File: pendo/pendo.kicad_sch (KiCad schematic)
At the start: 23 parts, among them J1 M2, J2 M1, J3 Motor Vin, J4 Conn_ARM_JTAG_SWD_10, SW1 SW_Push, U1 STM32G431RBTx, U2 DRV8870DDA, U3 DRV8870DDA, U4 ESP32-C3-WROOM-02, U5 AP2112K-3.3

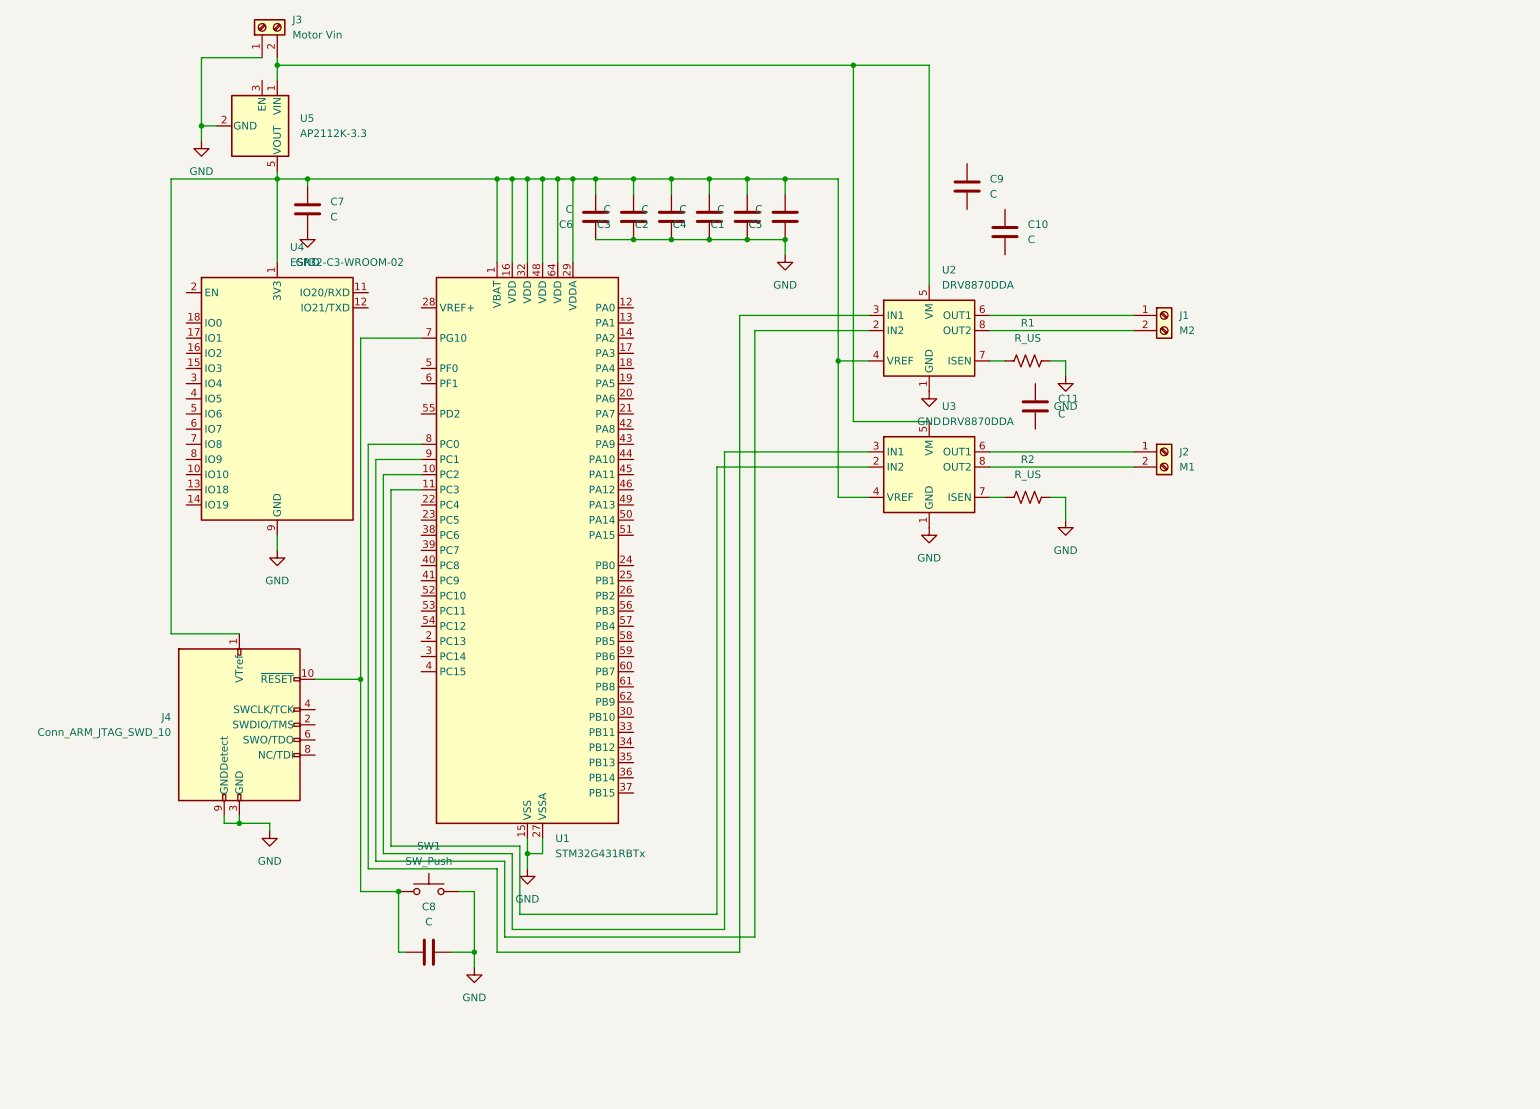
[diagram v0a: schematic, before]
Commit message: added caps and resistor values
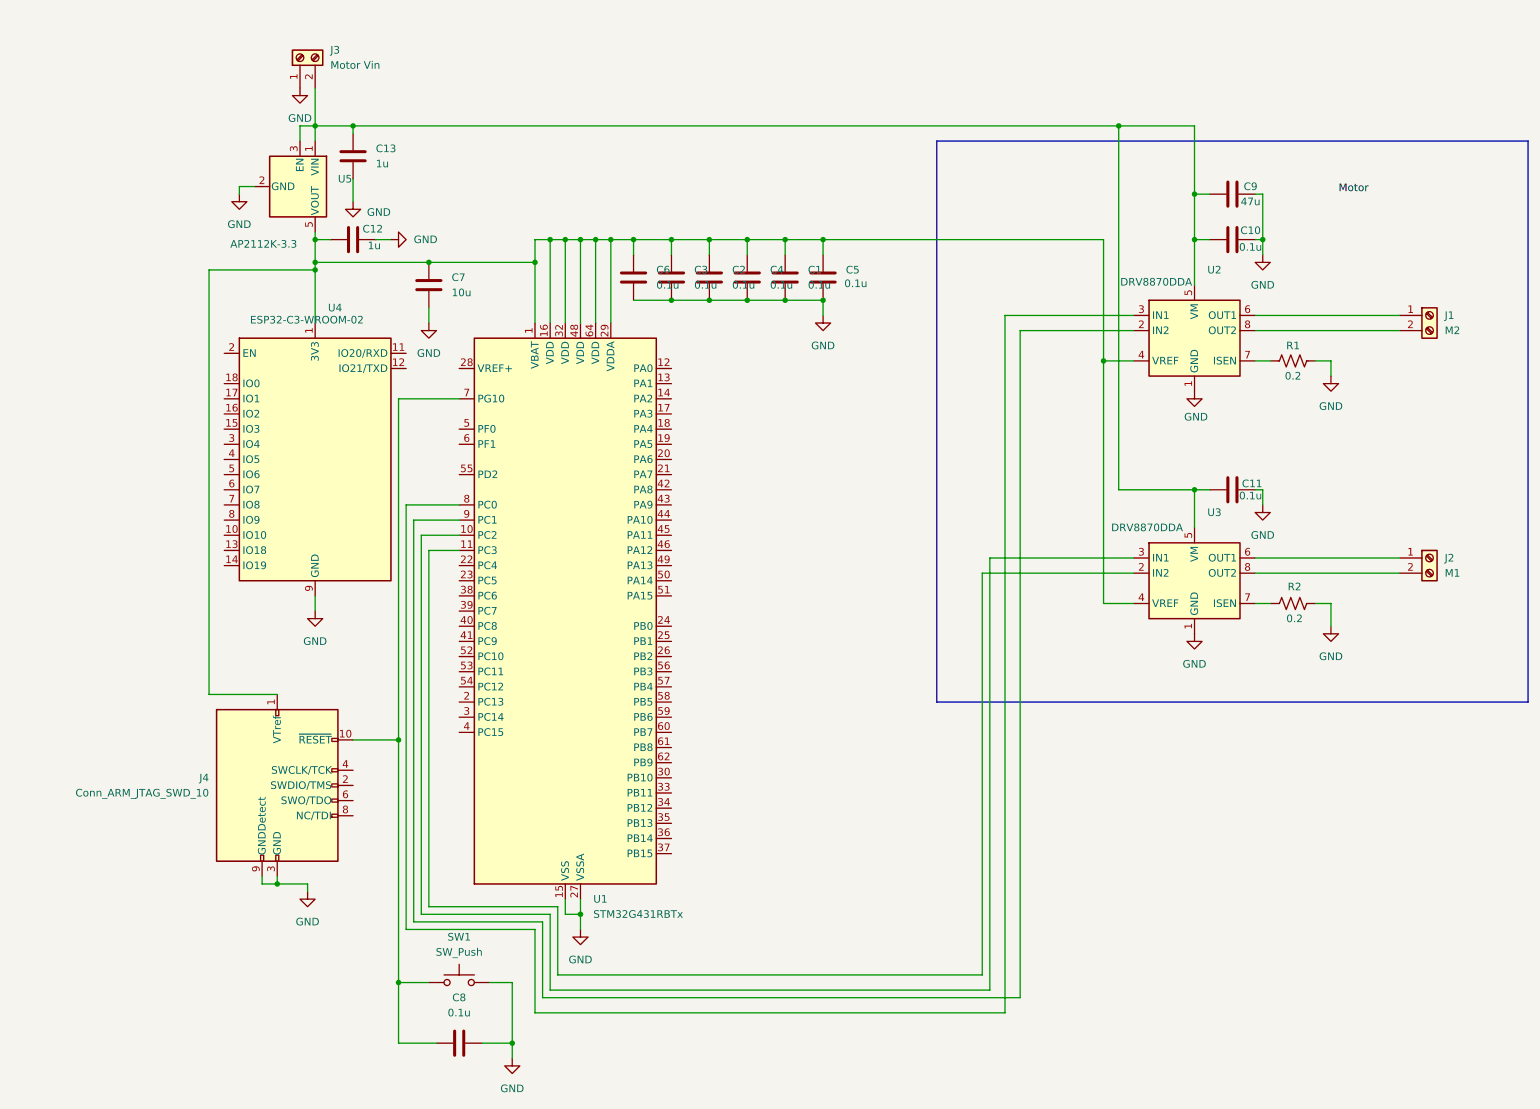
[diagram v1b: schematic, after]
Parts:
- added C12, C13: 1u, symbol Device:C
- C1, C10, C11, C2, C3, C4, C5, C6, C8: value C -> 0.1u
- C7: value C -> 10u
- C9: value C -> 47u
- R1, R2: value R_US -> 0.2
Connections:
- net GND: now also C10.2, C11.2, C9.2, C12.2, C13.2
- net at C1.2, C2.2, C3.2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: now also C12.1
- net at J3.2 (Pin_2), U2.5 (VM), U3.5 (VM)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: now also C10.1, C11.1, C9.1, U5.3 (EN), C13.1
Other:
- moved on the sheet: C1, C10, C11, C2, C3, C4, C5, C6, C7, C8, C9, J1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

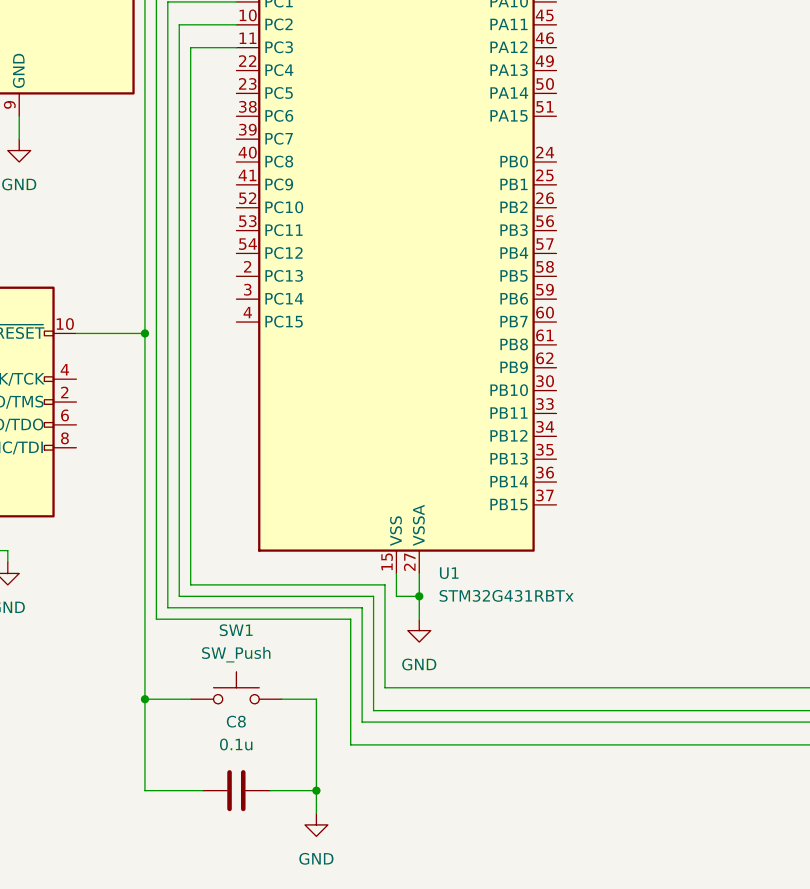
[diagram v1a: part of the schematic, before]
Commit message: adding i2c
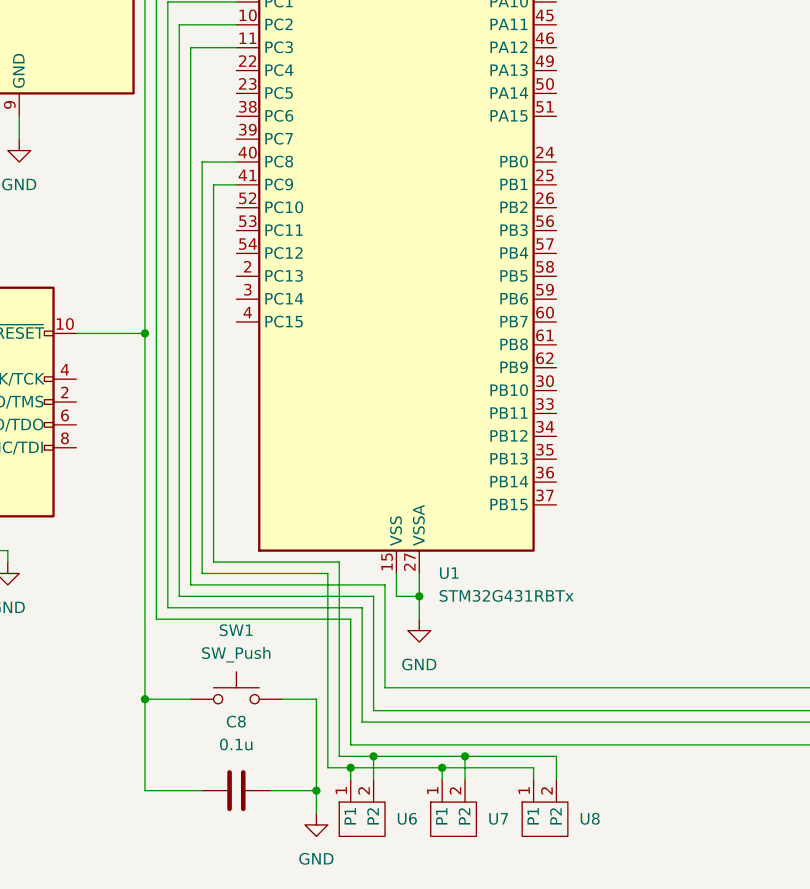
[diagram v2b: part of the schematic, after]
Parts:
- added U6, U7, U8: (no value), symbol Terminals:2pin
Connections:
- net at U1.40 (PC8): now also U6.1 (P1), U7.1 (P1), U8.1 (P1)
- net at U1.41 (PC9): now also U6.2 (P2), U7.2 (P2), U8.2 (P2)

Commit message: plane pours
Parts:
- C1, C12, C2, C3, C4, C5, C6, C7, C8: footprint (none) -> Capacitor_SMD:C_0603_1608Metric
- C10, C11, C13, C9: footprint (none) -> Capacitor_SMD:C_1206_3216Metric
- J1, J2, J3: footprint (none) -> TerminalBlock:TerminalBlock_MaiXu_MX126-5.0-02P_1x02_P5.00mm
- J4: footprint (none) -> Connector_PinHeader_1.27mm:PinHeader_2x05_P1.27mm_Vertical_SMD
- R1, R2: footprint (none) -> Resistor_SMD:R_0603_1608Metric
- SW1: footprint (none) -> Button_Switch_THT:SW_PUSH_6mm
- U6, U7, U8: footprint (none) -> Connector_PinHeader_2.54mm:PinHeader_1x02_P2.54mm_Vertical
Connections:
- net +3.3V: now reaches C1.2, C12.1, C2.2, C3.2, C4.2, C5.2, C6.2, C7.1, J4.1 (VTref), U1.1 (VBAT), U1.16 (VDD), U1.29 (VDDA), U1.32 (VDD), U1.48 (VDD), U1.64 (VDD), U2.4 (VREF), U3.4 (VREF), U4.1 (3V3), U5.5 (VOUT)
- net +12V: now reaches C10.1, C11.1, C13.1, C9.1, J3.2 (Pin_2), U2.5 (VM), U3.5 (VM), U5.1 (VIN), U5.3 (EN)

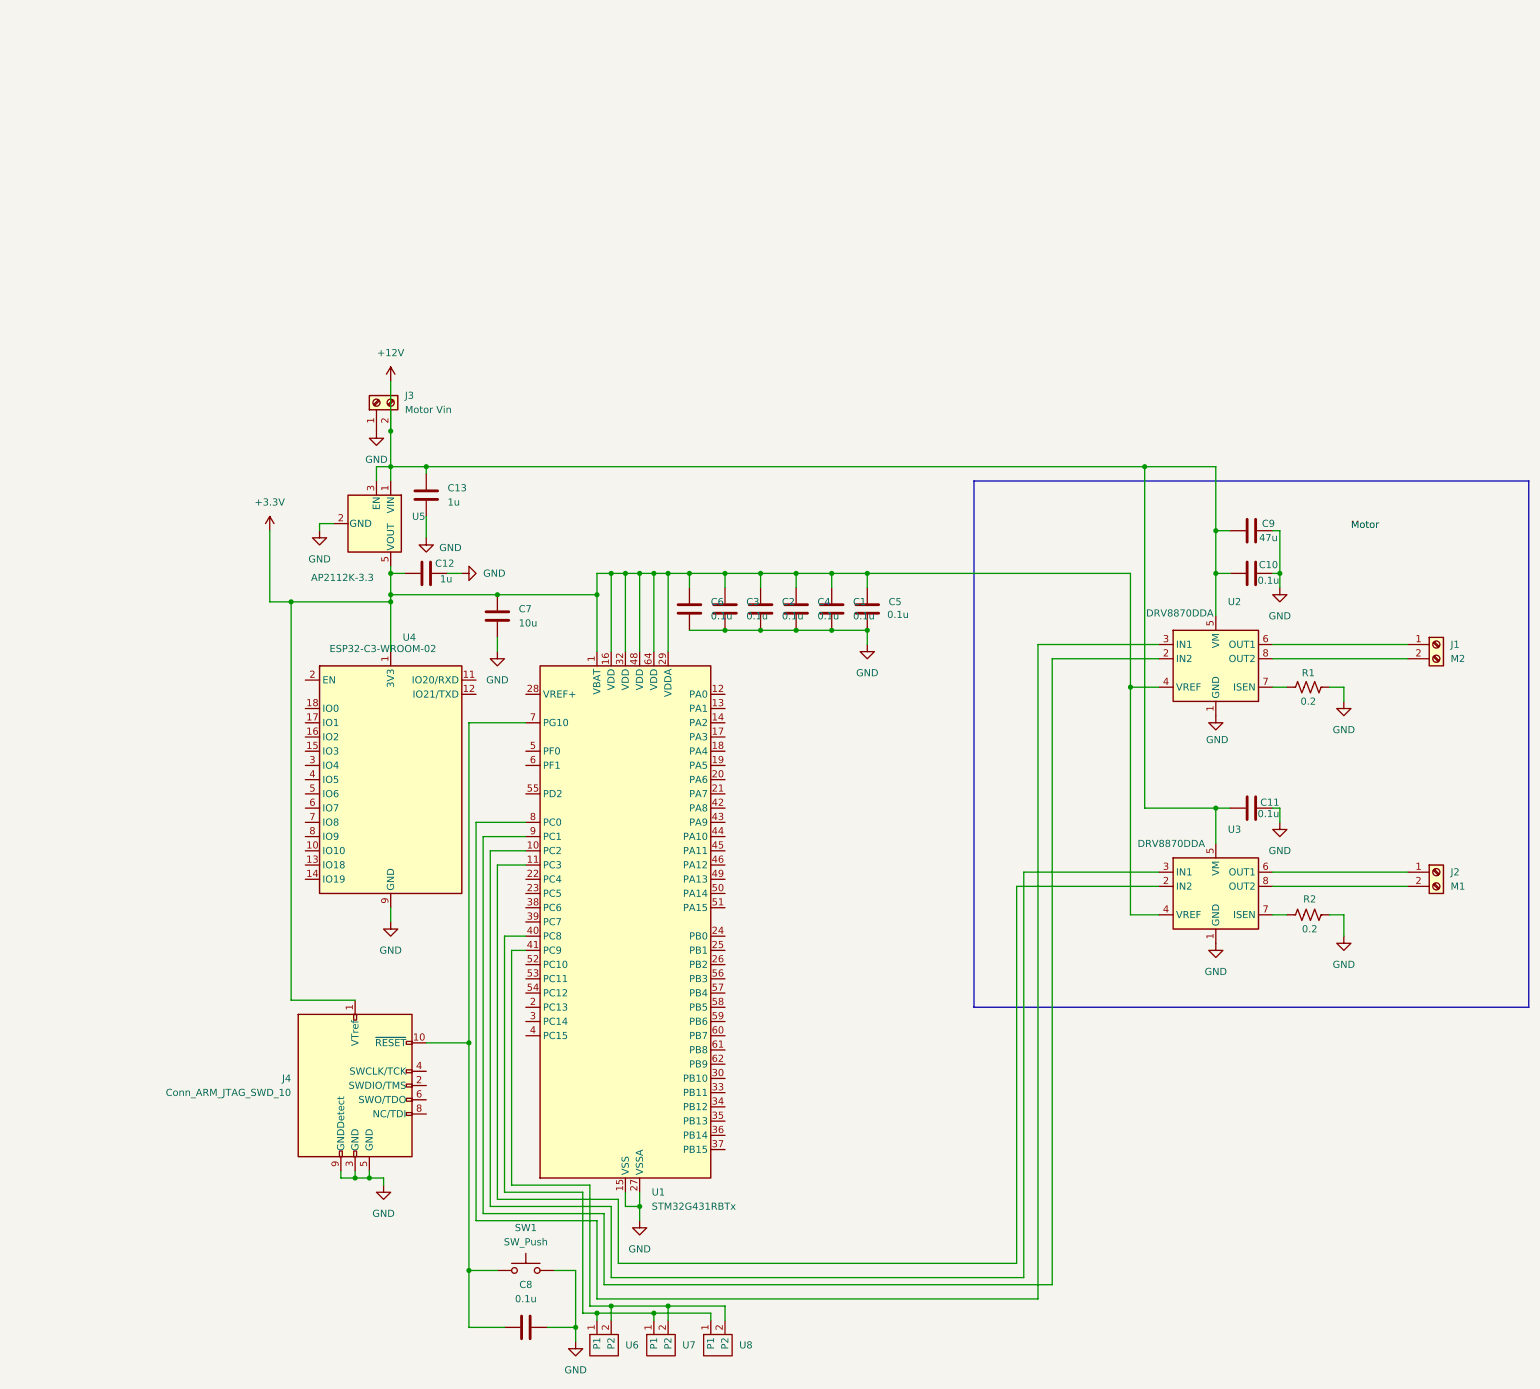
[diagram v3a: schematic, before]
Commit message: started gerber redesign + update power components
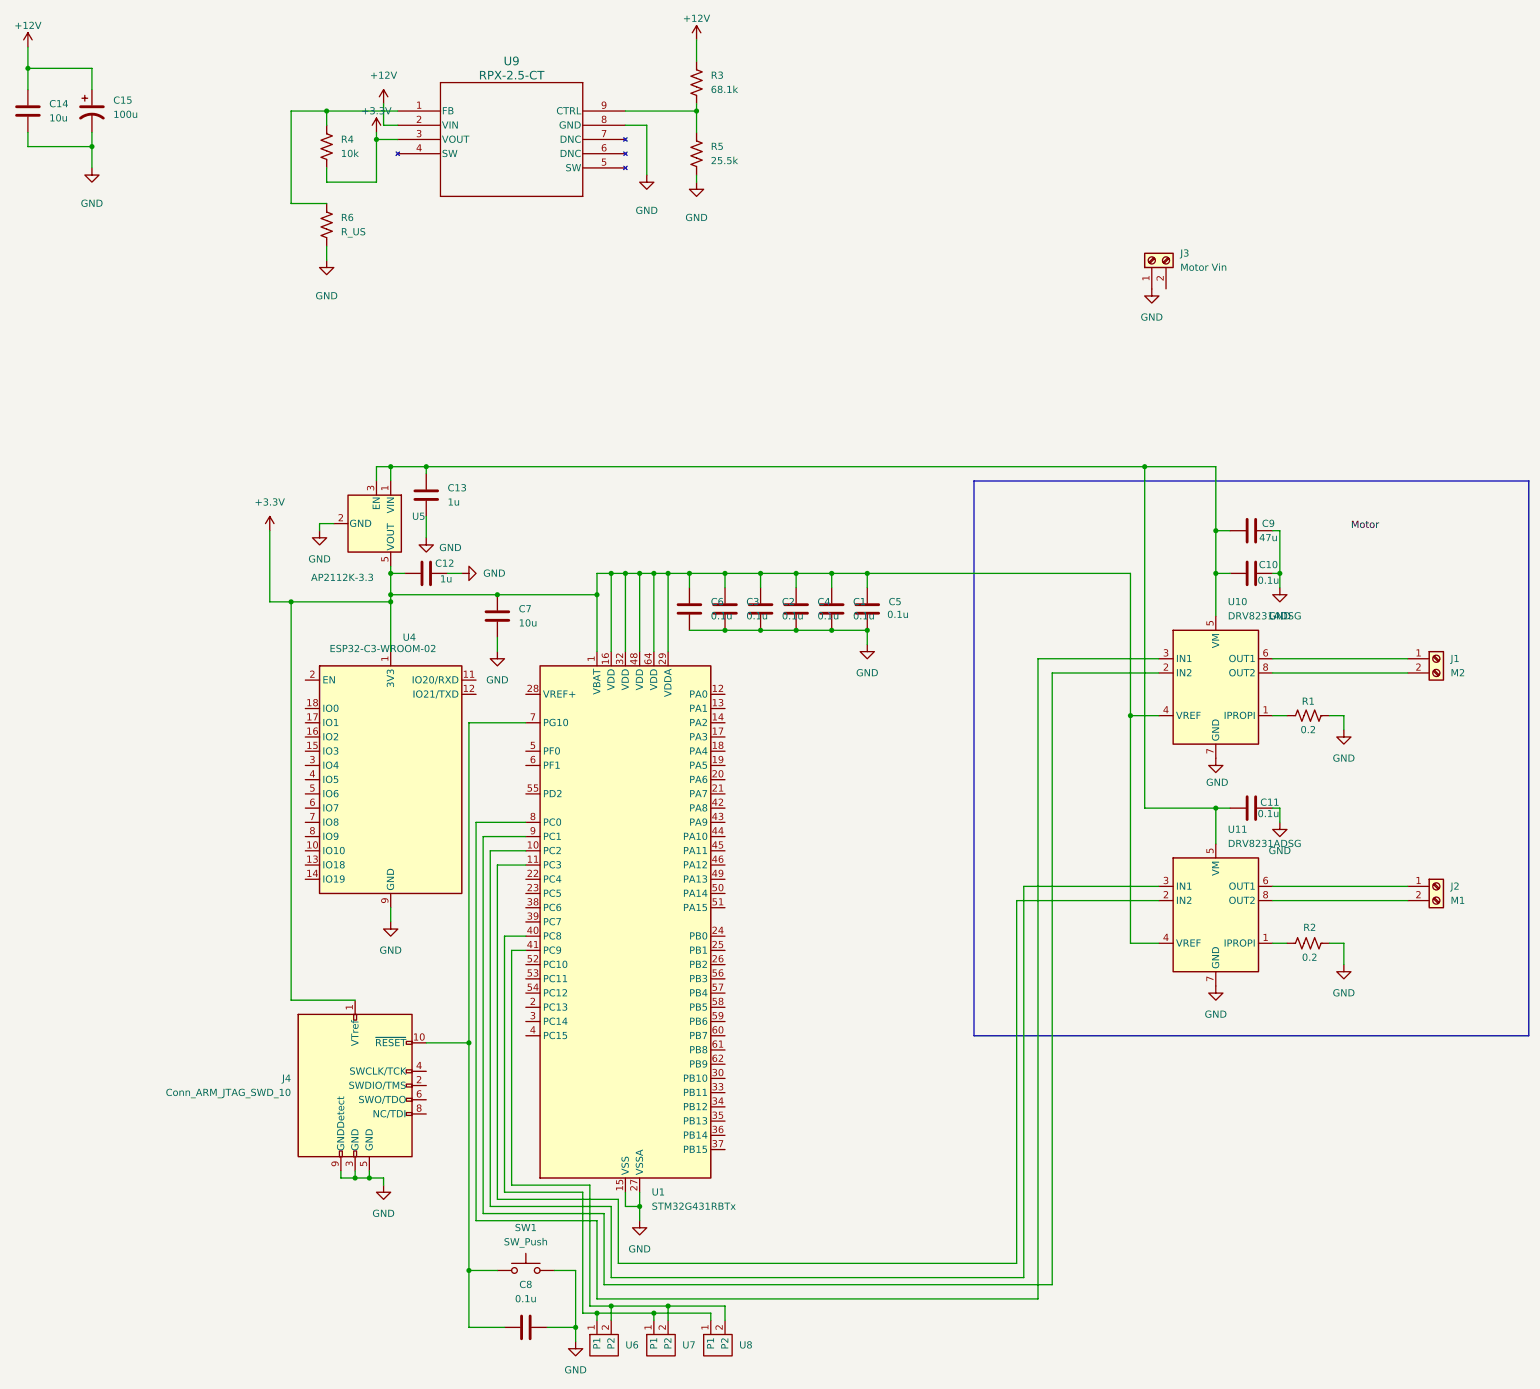
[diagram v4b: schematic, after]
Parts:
- removed U2, U3: DRV8870DDA, Package_SO:Texas_HTSOP-8-1EP_3.9x4.9mm_P1.27mm_EP2.95x4.9mm_Mask2.4x3.1mm_ThermalVias, symbol Driver_Motor:DRV8870DDA
- added C14: 10u, symbol Device:C
- added C15: 100u, symbol Device:C_Polarized_US
- added R3: 68.1k, symbol Device:R_US
- added R4: 10k, symbol Device:R_US
- added R5: 25.5k, symbol Device:R_US
- added R6: R_US, symbol Device:R_US
- added U10, U11: DRV8231ADSG, Package_SON:WSON-8-1EP_2x2mm_P0.5mm_EP0.9x1.6mm, symbol Driver_Motor:DRV8231ADSG
- added U9: RPX-2.5-CT, RPX-2.5, symbol 2026-04-20_18-04-11:RPX-2.5-CT
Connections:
- net +12V: now also C14.1, C15.1, R3.1, U9.2 (VIN); no longer C10.1, C11.1, C13.1, C9.1, J3.2 (Pin_2), U5.1 (VIN), U5.3 (EN)
- net +3.3V: now also R4.2, U10.4 (VREF), U11.4 (VREF), U9.3 (VOUT)
- net GND: now also C14.2, C15.2, R5.2, R6.2, U10.7 (GND), U10.9 (GND), U11.7 (GND), U11.9 (GND), U9.8 (GND)
- net at R2.1: now also U11.1 (IPROPI)
- net at U1.10 (PC2): now also U11.3 (IN1)
- net at U1.11 (PC3): now also U11.2 (IN2)
- net at U1.8 (PC0): now also U10.3 (IN1)
- net at U1.9 (PC1): now also U10.2 (IN2)
- net at J2.1 (Pin_1): now also U11.6 (OUT1)
- net at J2.2 (Pin_2): now also U11.8 (OUT2)
- net at J1.1 (Pin_1): now also U10.6 (OUT1)
- net at J1.2 (Pin_2): now also U10.8 (OUT2)
- net at R1.1: now also U10.1 (IPROPI)
- new net: C10.1, C11.1, C13.1, C9.1, U10.5 (VM), U11.5 (VM), U5.1 (VIN), U5.3 (EN)
- new net: R4.1, R6.1, U9.1 (FB)
- new net: R3.2, R5.1, U9.9 (CTRL)
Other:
- moved on the sheet: J1, J2, J3, R1, R2
